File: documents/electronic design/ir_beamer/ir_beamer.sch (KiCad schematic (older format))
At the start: 3 parts, among them P1 STM32F103_header

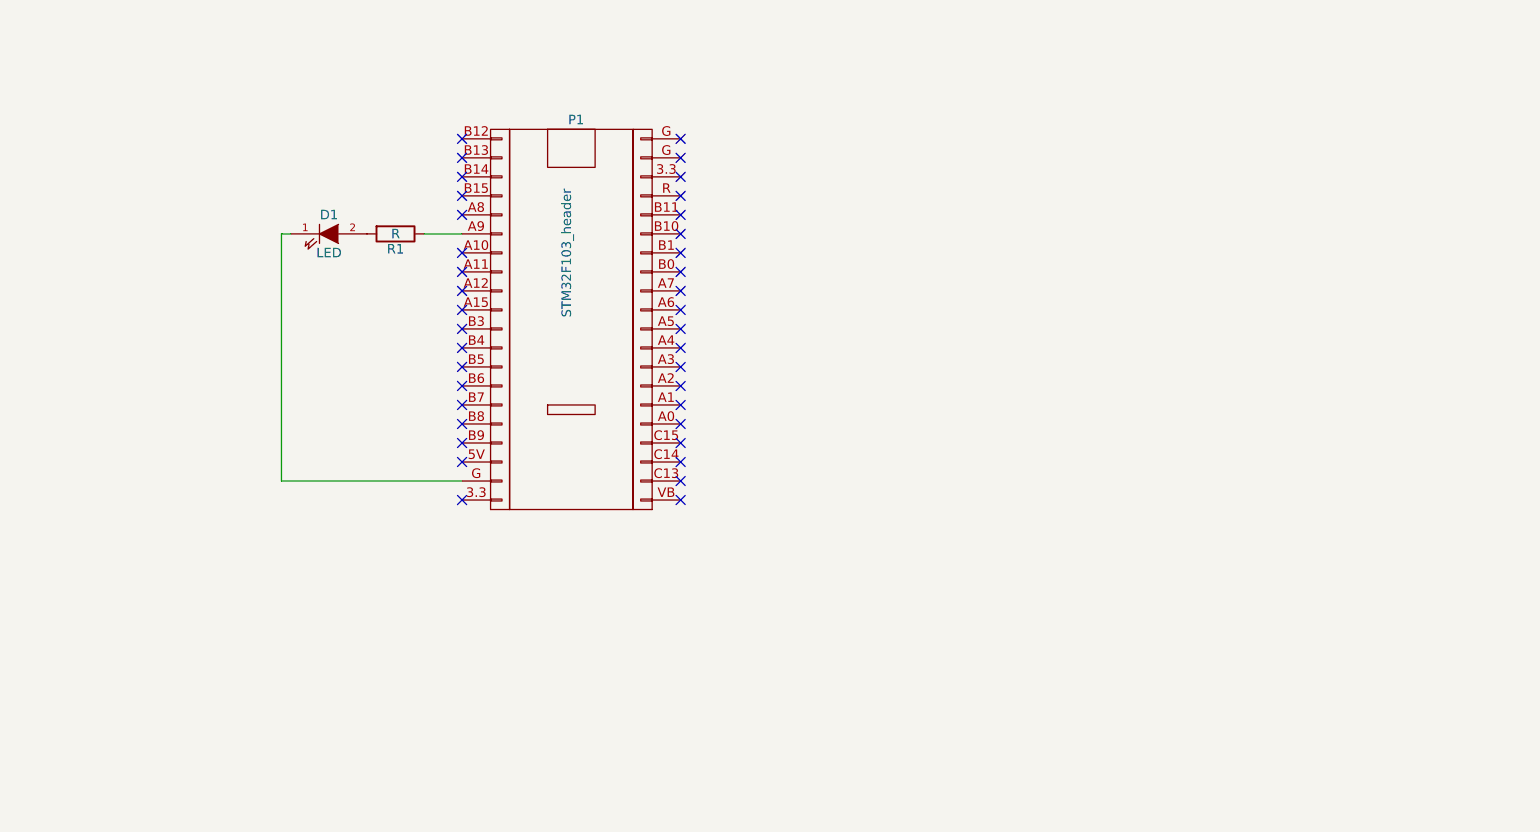
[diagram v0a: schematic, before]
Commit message: add project for testing 74hc595d with led
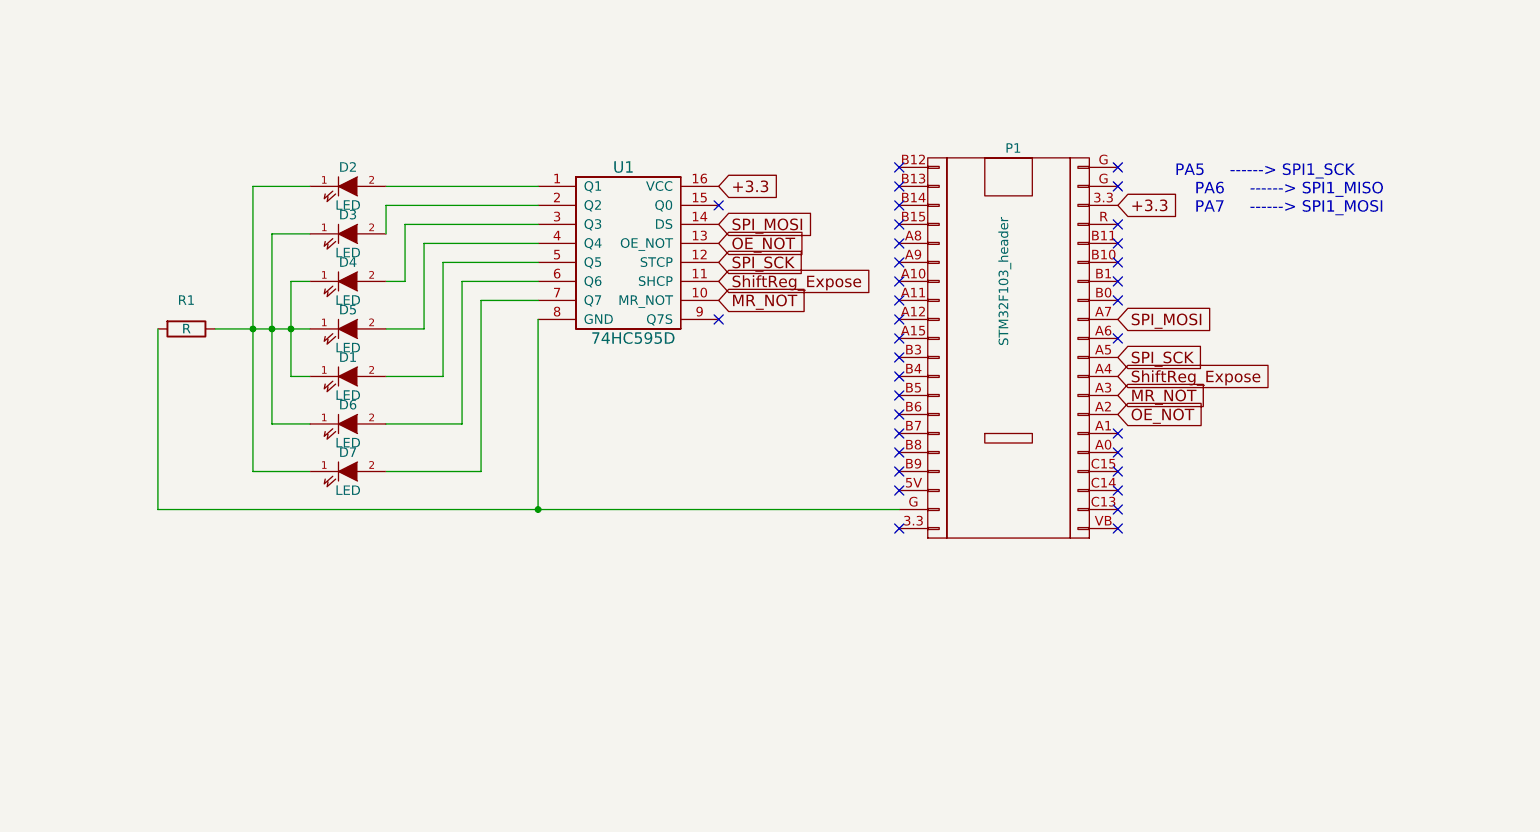
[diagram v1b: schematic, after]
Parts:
- added D2, D3, D4, D5, D6, D7: LED, LEDs:LED-5MM, symbol LED
- added U1: 74HC595D, footprints:74HC595D_SO16, symbol 74HC595D
- P1: footprint (none) -> footprints:STM32F103C8T6_pin_header
- R1: footprint (none) -> Resistors_SMD:R_0805_HandSoldering
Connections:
- net +3.3: now reaches P1.3.3
- net +3.3: now also U1.16 (VCC)
- net OE_NOT: now reaches P1.A2
- net OE_NOT: now also U1.13 (OE_NOT)
- net MR_NOT: now reaches P1.A3
- net MR_NOT: now also U1.10 (MR_NOT)
- net ShiftReg_Expose: now reaches P1.A4
- net ShiftReg_Expose: now also U1.11 (SHCP)
- net SPI_SCK: now reaches P1.A5
- net SPI_SCK: now also U1.12 (STCP)
- net SPI_MOSI: now reaches P1.A7
- net SPI_MOSI: now also U1.14 (DS)
- net at R1.1: now also D1.1 (K), D2.1 (K), D3.1 (K), D4.1 (K), D5.1 (K), D6.1 (K), D7.1 (K); no longer P1.A9
- net at D1.2 (A): now also U1.5 (Q5); no longer R1.2
- new net: P1.G, R1.2, U1.8 (GND)
- new net: D6.2 (A), U1.6 (Q6)
- new net: D7.2 (A), U1.7 (Q7)
- new net: D2.2 (A), U1.1 (Q1)
- new net: D3.2 (A), U1.2 (Q2)
- new net: D4.2 (A), U1.3 (Q3)
- new net: D5.2 (A), U1.4 (Q4)
- now unconnected: P1.G
- no-connect marks 38 -> 35
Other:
- note added: "PA5 ------> SPI1_SCK\n PA6 ------> SPI1_MISO\n PA7 ------> SPI1_MOSI"
- moved on the sheet: D1, R1

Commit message: update pcb
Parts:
- removed P1: STM32F103_header, footprints:STM32F103C8T6_pin_header, symbol STM32F103_header
- added U2: STM32F103HEADER, symbol STM32F103HEADER
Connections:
- net +3.3: now also U2.23 (+3.3V)
- net MR_NOT: now also U2.33 (A3)
- net OE_NOT: now also U2.34 (A2)
- net SPI_MOSI: now also U2.29 (A7)
- net SPI_SCK: now also U2.31 (A5)
- net ShiftReg_Expose: now also U2.32 (A4)
- net GND: now reaches R1.2, U1.8 (GND)
- net GND: now also U2.22 (GND)
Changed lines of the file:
@@
 NoConn ~ 5300 3050
 NoConn ~ 5300 3150
-NoConn ~ 6450 3350
-NoConn ~ 6450 3250
-NoConn ~ 6450 3150
-NoConn ~ 6450 3050
-NoConn ~ 6450 2950
-NoConn ~ 6450 2850
-NoConn ~ 6450 2150
-NoConn ~ 6450 1950
-NoConn ~ 6450 1850
-NoConn ~ 6450 1750
+NoConn ~ 6150 3350
+NoConn ~ 6150 3250
+NoConn ~ 6150 3150
+NoConn ~ 6150 3050
+NoConn ~ 6150 2950
+NoConn ~ 6150 2850
+NoConn ~ 6150 2150
+NoConn ~ 6150 1950
+NoConn ~ 6150 1850
+NoConn ~ 6150 1750
 $Comp
 L LED D1
@@
 	1    0    0    -1
 $EndComp
-$Comp
-L STM32F103_header P1
-U 1 1 578765C4
-P 5500 2400
-F 0 "P1" H 5900 3450 50  0000 C CNN
-F 1 "STM32F103_header" V 5850 2750 50  0000 C CNN
-F 2 "footprints:STM32F103C8T6_pin_header" H 5500 2400 50  0001 C CNN
-F 3 "" H 5500 2400 50  0000 C CNN
-	1    5500 2400
-	1    0    0    -1
-$EndComp
-Text Notes 6750 1700 0    60   ~ 0
+Text Notes 6450 1700 0    60   ~ 0
     PA5     ------> SPI1_SCK\n    PA6     ------> SPI1_MISO\n    PA7     ------> SPI1_MOSI
-Text GLabel 6450 2450 2    60   Input ~ 0
+Text GLabel 6150 2450 2    60   Input ~ 0
 SPI_SCK
-Text GLabel 6450 2250 2    60   Input ~ 0
+Text GLabel 6150 2250 2    60   Input ~ 0
 SPI_MOSI
 Text GLabel 4350 1950 2    60   Input ~ 0
@@
 Text GLabel 4350 1750 2    60   Input ~ 0
 SPI_MOSI
-Text GLabel 6450 2550 2    60   Input ~ 0
+Text GLabel 6150 2550 2    60   Input ~ 0
 ShiftReg_Expose
 Text GLabel 4350 2050 2    60   Input ~ 0
 ShiftReg_Expose
-Text GLabel 6450 1650 2    60   Input ~ 0
+Text GLabel 6150 1650 2    60   Input ~ 0
 +3.3
 Text GLabel 4350 1550 2    60   Input ~ 0
@@
 NoConn ~ 4350 2250
 NoConn ~ 4350 1650
-Text GLabel 6450 2750 2    60   Input ~ 0
+Text GLabel 6150 2750 2    60   Input ~ 0
 OE_NOT
-Text GLabel 6450 2650 2    60   Input ~ 0
+Text GLabel 6150 2650 2    60   Input ~ 0
 MR_NOT
 Text GLabel 4350 1850 2    60   Input ~ 0
@@
 MR_NOT
 NoConn ~ 5300 1950
-NoConn ~ 6450 2350
+NoConn ~ 6150 2350
 NoConn ~ 5300 3350
-NoConn ~ 6450 1450
-NoConn ~ 6450 1550
 Wire Wire Line
 	2600 1550 3400 1550
@@
 Wire Wire Line
 	1900 3050 2200 3050
-NoConn ~ 6450 2050
-Wire Wire Line
-	1400 3250 5300 3250
-Wire Wire Line
-	3400 3250 3400 2250
-Wire Wire Line
-	1400 2300 1400 3250
-Connection ~ 3400 3250
+NoConn ~ 6150 2050
+$Comp
+L GND #PWR01
+U 1 1 5787B950
+P 1400 2300
+F 0 "#PWR01" H 1400 2050 50  0001 C CNN
+F 1 "GND" H 1400 2150 50  0000 C CNN
+F 2 "" H 1400 2300 50  0000 C CNN
+F 3 "" H 1400 2300 50  0000 C CNN
+	1    1400 2300
+	0    1    1    0
+$EndComp
+$Comp
+L STM32F103HEADER U2
+U 1 1 5787BBF4
+P 5550 2500
+F 0 "U2" H 5700 3750 60  0000 C CNN
+F 1 "STM32F103HEADER" H 5750 1450 60  0000 C CNN
+F 2 "" H 4900 3500 60  0000 C CNN
+F 3 "" H 4900 3500 60  0000 C CNN
+	1    5550 2500
+	1    0    0    -1
+$EndComp
+$Comp
+L GND #PWR02
+U 1 1 5787C121
+P 3400 2250
+F 0 "#PWR02" H 3400 2000 50  0001 C CNN
+F 1 "GND" H 3400 2100 50  0000 C CNN
+F 2 "" H 3400 2250 50  0000 C CNN
+F 3 "" H 3400 2250 50  0000 C CNN
+	1    3400 2250
+	0    1    1    0
+$EndComp
+$Comp
+L GND #PWR03
+U 1 1 5787C14A
+P 6150 1550
+F 0 "#PWR03" H 6150 1300 50  0001 C CNN
+F 1 "GND" H 6150 1400 50  0000 C CNN
+F 2 "" H 6150 1550 50  0000 C CNN
+F 3 "" H 6150 1550 50  0000 C CNN
+	1    6150 1550
+	0    -1   -1   0
+$EndComp
+NoConn ~ 6150 1450
+NoConn ~ 5300 3250
 $EndSCHEMATC

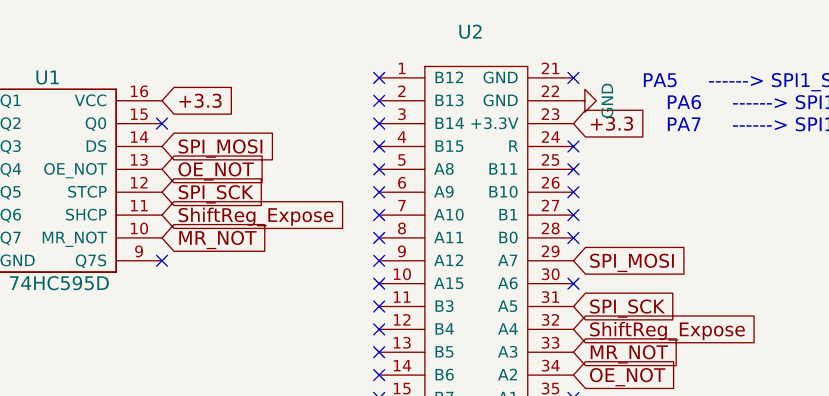
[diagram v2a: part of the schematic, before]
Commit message: fix pin numbers in ir_beamer
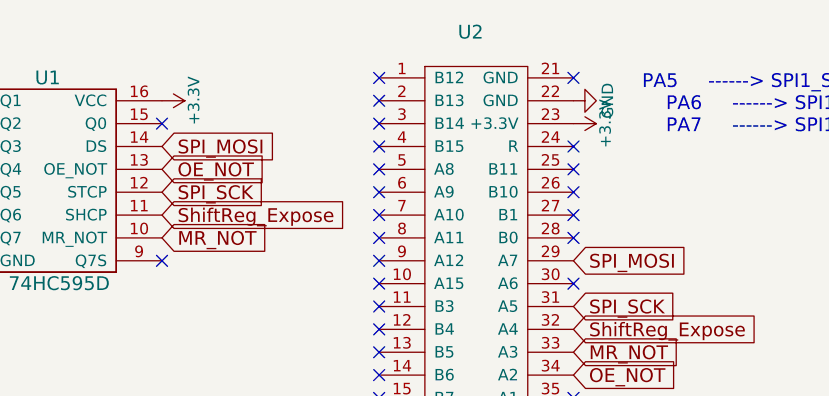
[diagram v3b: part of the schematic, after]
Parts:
- U2: footprint (none) -> footprints:STM32F103_header_footprint
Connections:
- net +3.3 renamed +3V3
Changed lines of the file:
@@
 Text GLabel 4350 2050 2    60   Input ~ 0
 ShiftReg_Expose
-Text GLabel 6150 1650 2    60   Input ~ 0
-+3.3
-Text GLabel 4350 1550 2    60   Input ~ 0
-+3.3
 NoConn ~ 4350 2250
 NoConn ~ 4350 1650
@@
 F 0 "U2" H 5700 3750 60  0000 C CNN
 F 1 "STM32F103HEADER" H 5750 1450 60  0000 C CNN
-F 2 "" H 4900 3500 60  0000 C CNN
+F 2 "footprints:STM32F103_header_footprint" H 4900 3500 60  0001 C CNN
 F 3 "" H 4900 3500 60  0000 C CNN
 	1    5550 2500
@@
 NoConn ~ 6150 1450
 NoConn ~ 5300 3250
+$Comp
+L +3.3V #PWR04
+U 1 1 5787EAA7
+P 6150 1650
+F 0 "#PWR04" H 6150 1500 50  0001 C CNN
+F 1 "+3.3V" H 6150 1790 50  0000 C CNN
+F 2 "" H 6150 1650 50  0000 C CNN
+F 3 "" H 6150 1650 50  0000 C CNN
+	1    6150 1650
+	0    1    1    0
+$EndComp
+$Comp
+L +3.3V #PWR05
+U 1 1 5787EAD7
+P 4350 1550
+F 0 "#PWR05" H 4350 1400 50  0001 C CNN
+F 1 "+3.3V" H 4350 1690 50  0000 C CNN
+F 2 "" H 4350 1550 50  0000 C CNN
+F 3 "" H 4350 1550 50  0000 C CNN
+	1    4350 1550
+	0    1    1    0
+$EndComp
 $EndSCHEMATC

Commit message: update pcb
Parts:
- removed R1: R, Resistors_SMD:R_0805_HandSoldering, symbol R
- added T1, T2, T3, T4, T5, T6, T7: 2N7002K, footprints:SOT23, symbol 2N7002K
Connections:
- net GND: now also U2.19 (GND), T1.2 (S), T2.2 (S), T3.2 (S), T4.2 (S), T5.2 (S), T6.2 (S), T7.2 (S); no longer U2.22 (GND)
- net IR_LED_5: now reaches U1.5 (Q5)
- net IR_LED_5: now also T5.1 (G); no longer D1.2 (A)
- net IR_LED_6: now reaches U1.6 (Q6)
- net IR_LED_6: now also T6.1 (G); no longer D6.2 (A)
- net IR_LED_7: now reaches U1.7 (Q7)
- net IR_LED_7: now also T7.1 (G); no longer D7.2 (A)
- net IR_LED_1: now reaches U1.1 (Q1)
- net IR_LED_1: now also T1.1 (G); no longer D2.2 (A)
- net IR_LED_2: now reaches U1.2 (Q2)
- net IR_LED_2: now also T2.1 (G); no longer D3.2 (A)
- net IR_LED_3: now reaches U1.3 (Q3)
- net IR_LED_3: now also T3.1 (G); no longer D4.2 (A)
- net IR_LED_4: now reaches U1.4 (Q4)
- net IR_LED_4: now also T4.1 (G); no longer D5.2 (A)
- net IR_PWM: now reaches U2.36 (A0)
- net IR_PWM: now also D1.2 (A), D2.2 (A), D3.2 (A), D4.2 (A), D5.2 (A), D6.2 (A), D7.2 (A)
- new net: D2.1 (K), T1.3 (D)
- new net: D1.1 (K), T2.3 (D)
- new net: D3.1 (K), T3.3 (D)
- new net: D4.1 (K), T4.3 (D)
- new net: D5.1 (K), T5.3 (D)
- new net: D6.1 (K), T6.3 (D)
- new net: D7.1 (K), T7.3 (D)
- no-connect marks 35 -> 34
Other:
- note added: "PA5 ------> SPI1_SCK\n PA6 ------> SPI1_MISO\n PA7 ------> SPI1_MOSI\n PA0 ------> IR_PWM (TIM2 CH1 PWM out)"
- note removed: "PA5 ------> SPI1_SCK\n PA6 ------> SPI1_MISO\n PA7 ------> SPI1_MOSI"
- moved on the sheet: D2, U1
